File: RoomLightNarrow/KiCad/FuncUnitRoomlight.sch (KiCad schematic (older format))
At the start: 34 parts, among them J11 PAD, J12 PAD, J13 PAD, J14 PAD, J15 PAD, J16 PAD, J17 PAD, J18 PAD, J19 PAD, J21 PAD, J22 PAD, Q11 SSM3K7002BFU, Q12 SSM3K7002BFU, Q13 SSM6N7002BFE, Q14 SSM6N7002BFE, Q17 SSM3K7002BFU

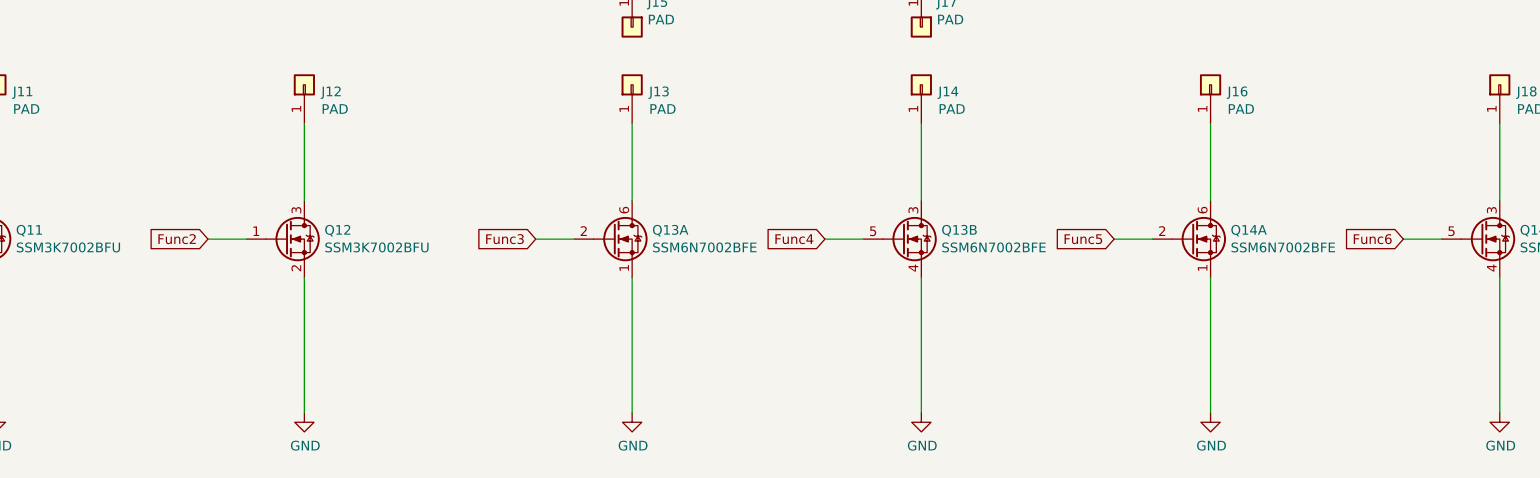
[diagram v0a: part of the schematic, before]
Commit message: 回路の問題点を修正 (K3066: Rev3 / それ以外: Rev2)
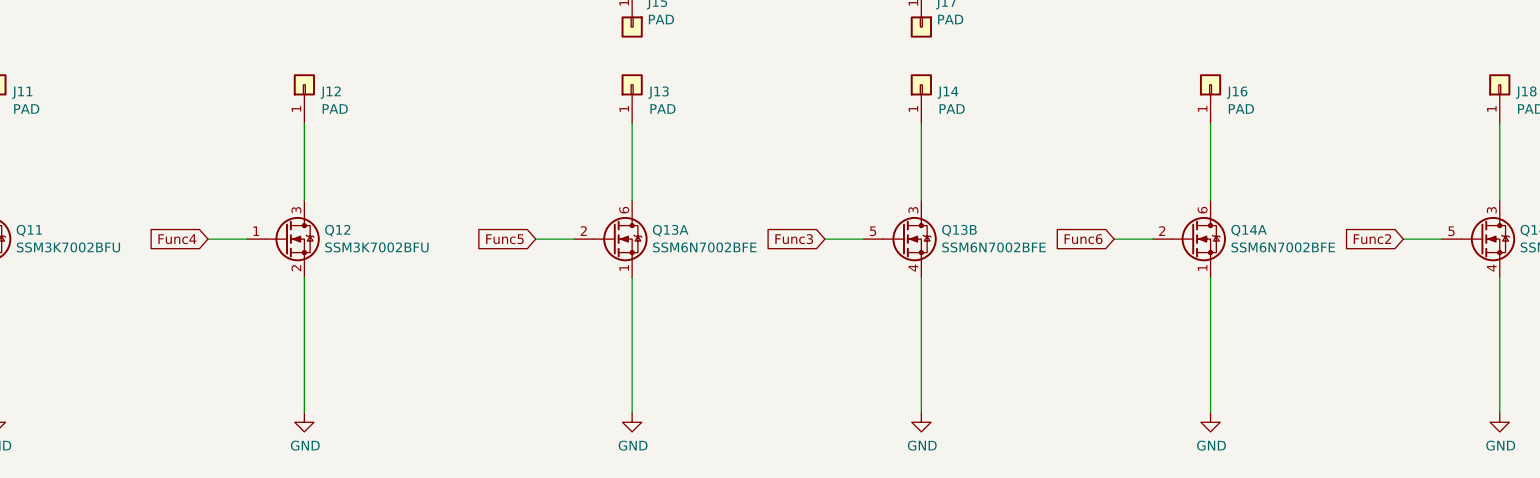
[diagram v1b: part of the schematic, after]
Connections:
- net Func2: now also Q14.5 (G); no longer Q12.1 (G)
- net Func3: now also Q13.5 (G); no longer Q13.2 (G)
- net Func4: now also Q12.1 (G); no longer Q13.5 (G)
- net Func5: now also Q13.2 (G); no longer Q14.2 (G)
- net Func6: now also Q14.2 (G); no longer Q14.5 (G)
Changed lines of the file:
@@
 	5300 2400 5300 2000
 Text GLabel 4800 2600 0    50   Input ~ 0
-Func3
+Func5
 Wire Wire Line
 	5000 2600 4800 2600
@@
 	6800 2400 6800 2000
 Text GLabel 6300 2600 0    50   Input ~ 0
-Func4
+Func3
 Wire Wire Line
 	6500 2600 6300 2600
@@
 	8300 2400 8300 2000
 Text GLabel 7800 2600 0    50   Input ~ 0
-Func5
+Func6
 Wire Wire Line
 	8000 2600 7800 2600
@@
 	9800 2400 9800 2000
 Text GLabel 9300 2600 0    50   Input ~ 0
-Func6
+Func2
 Wire Wire Line
 	9500 2600 9300 2600
@@
 	4650 5900 5050 5900
 Text GLabel 3100 2600 0    50   Input ~ 0
-Func2
+Func4
 Text GLabel 1500 2600 0    50   Input ~ 0
 Func1
